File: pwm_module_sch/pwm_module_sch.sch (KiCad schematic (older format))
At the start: 49 parts, among them J1 SWIMM, J2 output -, J3 input, J4 output+, J5 uart, Q1 AO3400, Q2 6N60, SW1 ., SW2 ., U1 TM1637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

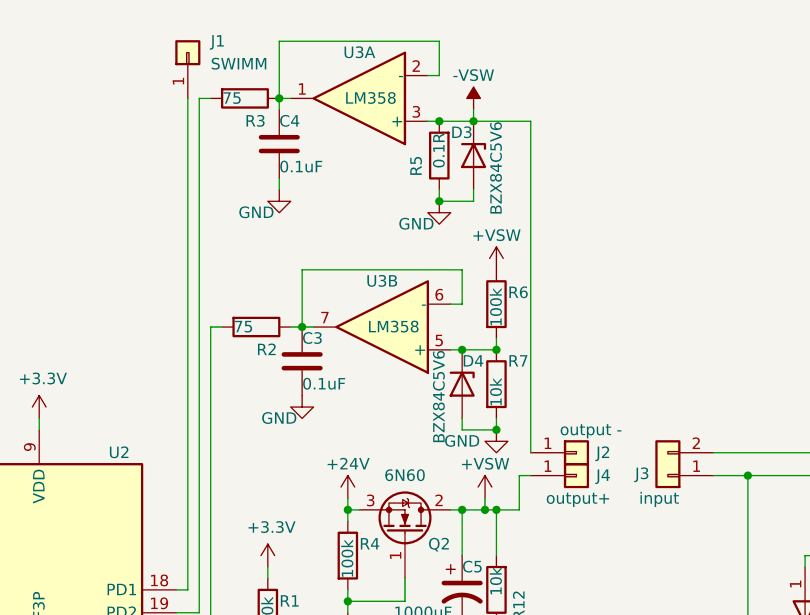
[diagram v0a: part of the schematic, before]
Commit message: 10A shunt
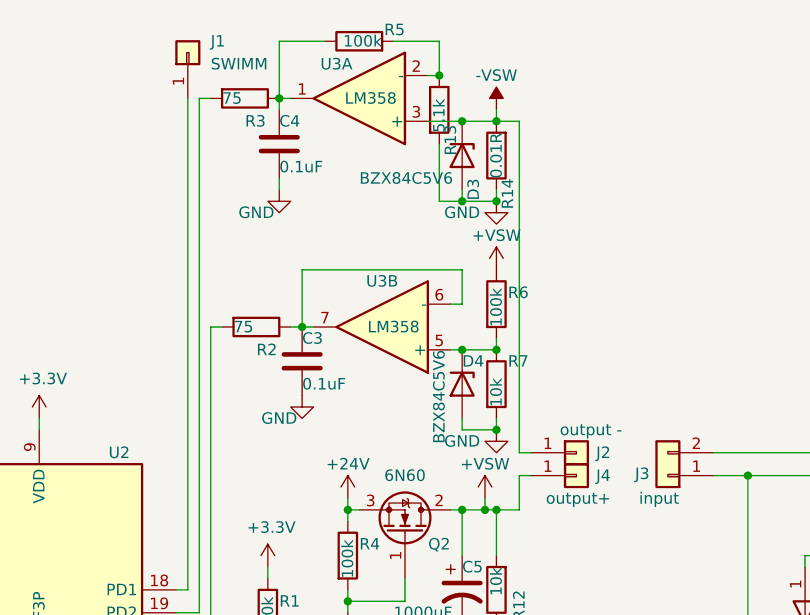
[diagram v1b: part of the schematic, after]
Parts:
- added R13: 5.1k, Resistor_SMD:R_0805_2012Metric, symbol Device:R
- added R14: 0.01R, Resistor_THT:R_Bare_Metal_Element_L12.4mm_W4.8mm_P11.40mm, symbol Device:R
- R5: value 0.1R -> 100k; footprint Resistor_SMD:R_1210_3225Metric -> Resistor_SMD:R_0402_1005Metric
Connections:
- net -VSW: now also R14.2; no longer R5.2
- net GND: now also R13.2, R14.1; no longer R5.1
- net at C4.1, R3.1, U3.1: now also R5.1; no longer U3.2 (-)
- new net: R13.1, R5.2, U3.2 (-)
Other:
- moved on the sheet: D3
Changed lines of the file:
@@
 U 1 1 62109DDC
 P 4750 800
-F 0 "U3" H 4750 600 50  0000 C CNN
+F 0 "U3" H 4850 650 50  0000 C CNN
 F 1 "LM358" H 4700 800 50  0000 C CNN
 F 2 "Package_SO:SO-8_3.9x4.9mm_P1.27mm" H 4750 800 50  0001 C CNN
@@
 	5100 700  5100 550
 Wire Wire Line
-	5100 550  4400 550
-Wire Wire Line
 	4400 550  4400 800
 Wire Wire Line
 	4400 800  4450 800
-$Comp
-L Device:R R5
-U 1 1 62070859
-P 5100 1050
-F 0 "R5" V 5200 1050 50  0000 L CNN
-F 1 "0.1R" V 5100 950 50  0000 L CNN
-F 2 "Resistor_SMD:R_1210_3225Metric" V 5030 1050 50  0001 C CNN
-F 3 "~" H 5100 1050 50  0001 C CNN
-	1    5100 1050
-	-1   0    0    1
-$EndComp
-Wire Wire Line
-	5100 900  5050 900
 $Comp
 L power:GND #PWR0107
 U 1 1 6208BD4F
-P 5100 1250
-F 0 "#PWR0107" H 5100 1000 50  0001 C CNN
-F 1 "GND" H 5000 1150 50  0000 C CNN
-F 2 "" H 5100 1250 50  0001 C CNN
-F 3 "" H 5100 1250 50  0001 C CNN
-	1    5100 1250
+P 5350 1250
+F 0 "#PWR0107" H 5350 1000 50  0001 C CNN
+F 1 "GND" H 5200 1200 50  0000 C CNN
+F 2 "" H 5350 1250 50  0001 C CNN
+F 3 "" H 5350 1250 50  0001 C CNN
+	1    5350 1250
 	1    0    0    -1
 $EndComp
@@
 L power:-VSW #PWR0132
 U 1 1 6210BE8B
-P 5250 850
-F 0 "#PWR0132" H 5250 950 50  0001 C CNN
-F 1 "-VSW" H 5250 1000 50  0000 C CNN
-F 2 "" H 5250 850 50  0001 C CNN
-F 3 "" H 5250 850 50  0001 C CNN
-	1    5250 850
+P 5350 850
+F 0 "#PWR0132" H 5350 950 50  0001 C CNN
+F 1 "-VSW" H 5350 1000 50  0000 C CNN
+F 2 "" H 5350 850 50  0001 C CNN
+F 3 "" H 5350 850 50  0001 C CNN
+	1    5350 850
 	1    0    0    -1
 $EndComp
@@
 L Diode:BZX84Cxx D3
 U 1 1 622739ED
-P 5250 1050
-F 0 "D3" V 5150 950 50  0000 L CNN
-F 1 "BZX84C5V6" H 5100 1150 50  0000 L CNN
-F 2 "Diode_SMD:D_SOT-23_ANK" H 5250 875 50  0001 C CNN
-F 3 "https://diotec.com/tl_files/diotec/files/pdf/datasheets/bzx84c2v4.pdf" H 5250 1050 50  0001 C CNN
-	1    5250 1050
+P 5200 1050
+F 0 "D3" H 5300 1100 50  0000 L CNN
+F 1 "BZX84C5V6" V 5300 600 50  0000 L CNN
+F 2 "Diode_SMD:D_SOT-23_ANK" H 5200 875 50  0001 C CNN
+F 3 "https://diotec.com/tl_files/diotec/files/pdf/datasheets/bzx84c2v4.pdf" H 5200 1050 50  0001 C CNN
+	1    5200 1050
 	0    1    1    0
 $EndComp
-Wire Wire Line
-	5100 900  5250 900
-Connection ~ 5100 900
-Wire Wire Line
-	5100 1200 5100 1250
-Wire Wire Line
-	5250 1200 5250 1250
-Wire Wire Line
-	5250 1250 5100 1250
-Connection ~ 5100 1250
-Connection ~ 5250 900
 $Comp
 L Device:C C4
@@
 	1    0    0    -1
 $EndComp
-Wire Wire Line
-	5250 900  5250 850
 Wire Wire Line
 	2400 4300 2400 4200
@@
 	4050 800  4050 3050
 Wire Wire Line
-	5500 900  5500 2350
-Wire Wire Line
-	5250 900  5500 900
-Wire Wire Line
 	4000 800  4000 2950
+$Comp
+L Device:R R14
+U 1 1 622FAFE9
+P 5350 1050
+F 0 "R14" V 5300 1150 50  0000 L CNN
+F 1 "0.01R" V 5350 950 50  0000 L CNN
+F 2 "Resistor_THT:R_Bare_Metal_Element_L12.4mm_W4.8mm_P11.40mm" V 5280 1050 50  0001 C CNN
+F 3 "~" H 5350 1050 50  0001 C CNN
+	1    5350 1050
+	-1   0    0    1
+$EndComp
+Connection ~ 5200 900
+Wire Wire Line
+	5200 1200 5200 1250
+Wire Wire Line
+	5450 2350 5500 2350
+Wire Wire Line
+	5200 900  5350 900
+Wire Wire Line
+	5450 900  5450 2350
+$Comp
+L Device:R R5
+U 1 1 62418FC9
+P 4750 550
+F 0 "R5" V 4800 350 50  0000 L CNN
+F 1 "100k" V 4750 450 50  0000 L CNN
+F 2 "Resistor_SMD:R_0402_1005Metric" V 4680 550 50  0001 C CNN
+F 3 "~" H 4750 550 50  0001 C CNN
+	1    4750 550
+	0    -1   -1   0
+$EndComp
+Connection ~ 5350 900
+Wire Wire Line
+	5350 900  5450 900
+Wire Wire Line
+	5200 1250 5350 1250
+Wire Wire Line
+	5050 900  5200 900
+Wire Wire Line
+	5350 1250 5350 1200
+Connection ~ 5350 1250
+$Comp
+L Device:R R13
+U 1 1 62467885
+P 5100 850
+F 0 "R13" V 5150 650 50  0000 L CNN
+F 1 "5.1k" V 5100 750 50  0000 L CNN
+F 2 "Resistor_SMD:R_0805_2012Metric" V 5030 850 50  0001 C CNN
+F 3 "~" H 5100 850 50  0001 C CNN
+	1    5100 850
+	1    0    0    -1
+$EndComp
+Connection ~ 5100 700
+Wire Wire Line
+	5100 1000 5100 1250
+Wire Wire Line
+	5100 1250 5200 1250
+Connection ~ 5200 1250
+Wire Wire Line
+	5350 900  5350 850
+Wire Wire Line
+	4400 550  4600 550
+Wire Wire Line
+	4900 550  5100 550
 $EndSCHEMATC

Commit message: board ok
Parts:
- Q2: value 6N60 -> IRFZ44N
- R12: footprint Resistor_SMD:R_1210_3225Metric -> Resistor_SMD:R_1206_3216Metric
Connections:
- net GND: now also R13.1; no longer R13.2
- net at R5.2, U3.2 (-): now also R13.2; no longer R13.1
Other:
- moved on the sheet: C7, C8, C9, D3, D8, R13, R14, R8, U4

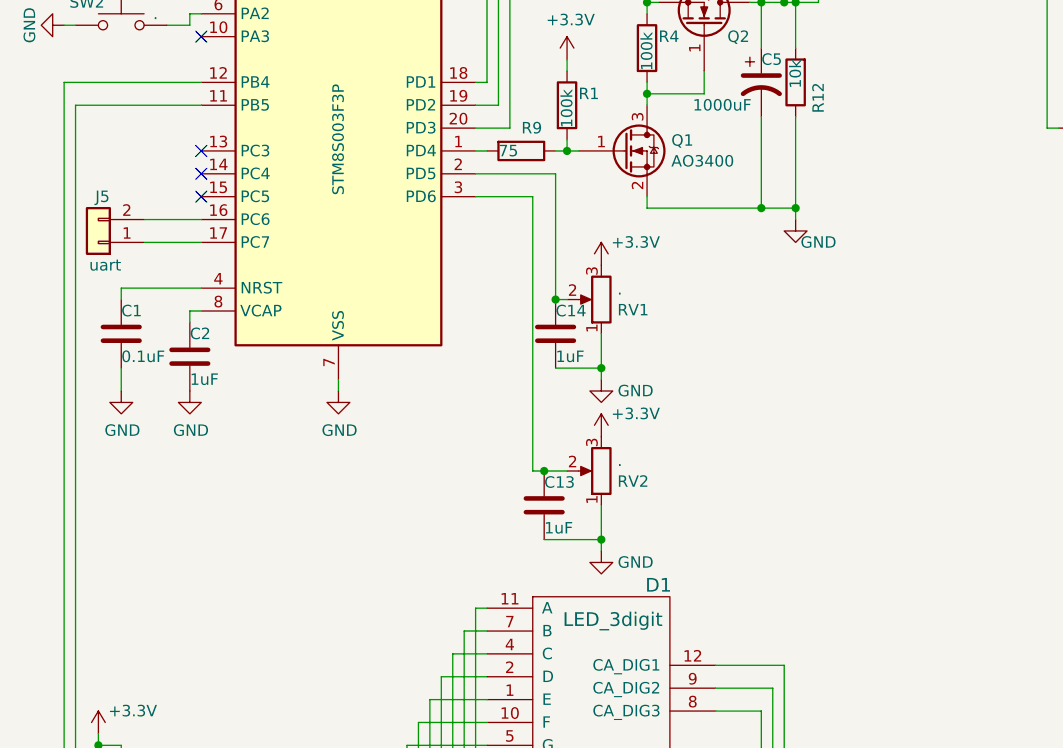
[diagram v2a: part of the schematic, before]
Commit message: working UART on board
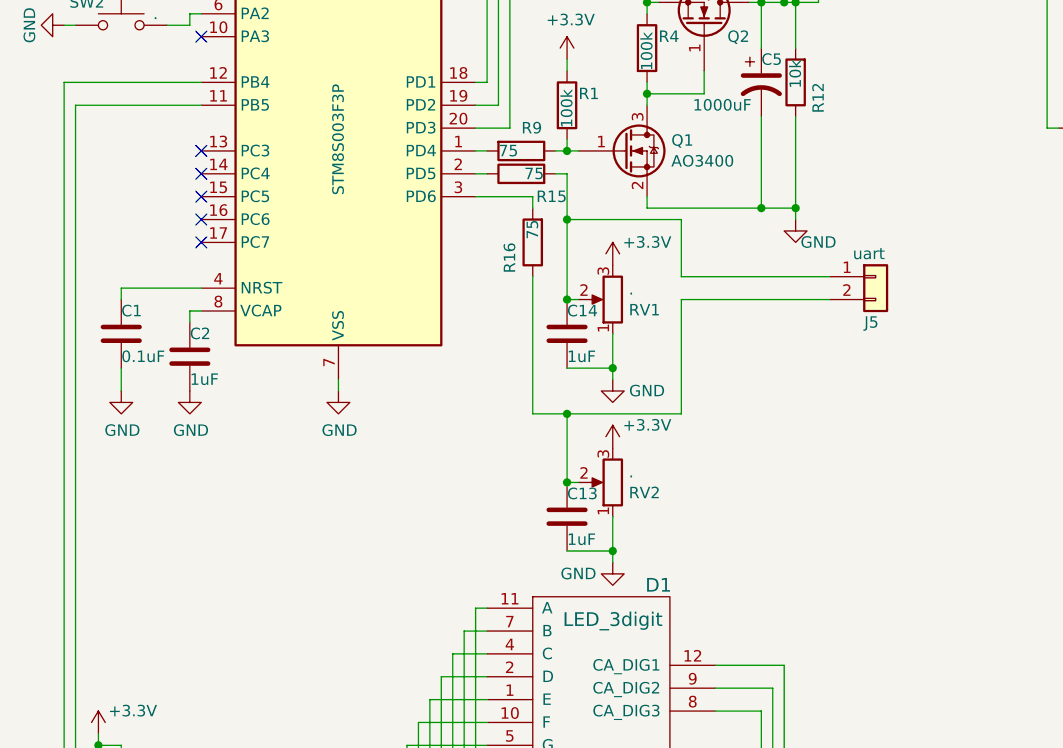
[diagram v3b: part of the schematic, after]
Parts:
- added R15, R16: 75, Resistor_SMD:R_0402_1005Metric, symbol Device:R
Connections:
- net at U2.16 (PC6): no longer J5.2 (Pin_2)
- net at U2.17 (PC7): no longer J5.1 (Pin_1)
- net at C14.1, RV1.2: now also J5.1 (Pin_1), R15.2; no longer U2.2 (PD5)
- net at C13.1, RV2.2: now also J5.2 (Pin_2), R16.1; no longer U2.3 (PD6)
- new net: R15.1, U2.2 (PD5)
- new net: R16.2, U2.3 (PD6)
- no-connect marks 6 -> 8
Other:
- moved on the sheet: C13, C14, J5, RV1, RV2
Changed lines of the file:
@@
 L power:GND #PWR0105
 U 1 1 620B76D5
-P 4500 4250
-F 0 "#PWR0105" H 4500 4000 50  0001 C CNN
-F 1 "GND" H 4650 4200 50  0000 C CNN
-F 2 "" H 4500 4250 50  0001 C CNN
-F 3 "" H 4500 4250 50  0001 C CNN
-	1    4500 4250
+P 4550 4250
+F 0 "#PWR0105" H 4550 4000 50  0001 C CNN
+F 1 "GND" H 4700 4200 50  0000 C CNN
+F 2 "" H 4550 4250 50  0001 C CNN
+F 3 "" H 4550 4250 50  0001 C CNN
+	1    4550 4250
 	1    0    0    -1
 $EndComp
@@
 L Device:R_Potentiometer RV1
 U 1 1 620D21AF
-P 4500 3900
-F 0 "RV1" H 4430 3946 50  0000 R CNN
-F 1 "." H 4430 3855 50  0000 R CNN
-F 2 "pwm_module:SP3-4" H 4500 3900 50  0001 C CNN
-F 3 "~" H 4500 3900 50  0001 C CNN
-	1    4500 3900
+P 4550 3900
+F 0 "RV1" H 4480 3946 50  0000 R CNN
+F 1 "." H 4480 3855 50  0000 R CNN
+F 2 "pwm_module:SP3-4" H 4550 3900 50  0001 C CNN
+F 3 "~" H 4550 3900 50  0001 C CNN
+	1    4550 3900
 	-1   0    0    1
 $EndComp
@@
 L Device:R_Potentiometer RV2
 U 1 1 620D31F7
-P 4500 4650
-F 0 "RV2" H 4430 4696 50  0000 R CNN
-F 1 "." H 4430 4605 50  0000 R CNN
-F 2 "pwm_module:SP3-4" H 4500 4650 50  0001 C CNN
-F 3 "~" H 4500 4650 50  0001 C CNN
-	1    4500 4650
+P 4550 4700
+F 0 "RV2" H 4480 4746 50  0000 R CNN
+F 1 "." H 4480 4655 50  0000 R CNN
+F 2 "pwm_module:SP3-4" H 4550 4700 50  0001 C CNN
+F 3 "~" H 4550 4700 50  0001 C CNN
+	1    4550 4700
 	-1   0    0    1
 $EndComp
@@
 L power:+3.3V #PWR0114
 U 1 1 622371EC
-P 4500 3750
-F 0 "#PWR0114" H 4500 3600 50  0001 C CNN
-F 1 "+3.3V" H 4650 3850 50  0000 C CNN
-F 2 "" H 4500 3750 50  0001 C CNN
-F 3 "" H 4500 3750 50  0001 C CNN
-	1    4500 3750
+P 4550 3750
+F 0 "#PWR0114" H 4550 3600 50  0001 C CNN
+F 1 "+3.3V" H 4700 3850 50  0000 C CNN
+F 2 "" H 4550 3750 50  0001 C CNN
+F 3 "" H 4550 3750 50  0001 C CNN
+	1    4550 3750
 	1    0    0    -1
 $EndComp
@@
 L power:+3.3V #PWR0115
 U 1 1 6223863E
-P 4500 4500
-F 0 "#PWR0115" H 4500 4350 50  0001 C CNN
-F 1 "+3.3V" H 4650 4600 50  0000 C CNN
-F 2 "" H 4500 4500 50  0001 C CNN
-F 3 "" H 4500 4500 50  0001 C CNN
-	1    4500 4500
+P 4550 4550
+F 0 "#PWR0115" H 4550 4400 50  0001 C CNN
+F 1 "+3.3V" H 4700 4650 50  0000 C CNN
+F 2 "" H 4550 4550 50  0001 C CNN
+F 3 "" H 4550 4550 50  0001 C CNN
+	1    4550 4550
 	1    0    0    -1
 $EndComp
@@
 L power:GND #PWR0117
 U 1 1 6223B781
-P 4500 5000
-F 0 "#PWR0117" H 4500 4750 50  0001 C CNN
-F 1 "GND" H 4650 4950 50  0000 C CNN
-F 2 "" H 4500 5000 50  0001 C CNN
-F 3 "" H 4500 5000 50  0001 C CNN
-	1    4500 5000
-	1    0    0    -1
-$EndComp
-Wire Wire Line
-	4350 3900 4300 3900
+P 4550 5050
+F 0 "#PWR0117" H 4550 4800 50  0001 C CNN
+F 1 "GND" H 4400 5000 50  0000 C CNN
+F 2 "" H 4550 5050 50  0001 C CNN
+F 3 "" H 4550 5050 50  0001 C CNN
+	1    4550 5050
+	1    0    0    -1
+$EndComp
+Wire Wire Line
+	4400 3900 4350 3900
 Wire Wire Line
 	3950 3450 4200 3450
-Wire Wire Line
-	4250 4650 4350 4650
 Wire Wire Line
 	4100 3150 3950 3150
@@
 	1    0    0    -1
 $EndComp
-$Comp
-L Device:C C13
-U 1 1 62262A8F
-P 4250 4800
-F 0 "C13" H 4250 4900 50  0000 L CNN
-F 1 "1uF" H 4250 4700 50  0000 L CNN
-F 2 "Capacitor_SMD:C_0805_2012Metric" H 4288 4650 50  0001 C CNN
-F 3 "~" H 4250 4800 50  0001 C CNN
-	1    4250 4800
-	1    0    0    -1
-$EndComp
-Wire Wire Line
-	4250 4950 4500 4950
-Wire Wire Line
-	4500 4950 4500 5000
-Wire Wire Line
-	4500 4950 4500 4800
-Connection ~ 4500 4950
+Wire Wire Line
+	4550 5000 4550 5050
+Wire Wire Line
+	4550 5000 4550 4850
+Connection ~ 4550 5000
 $Comp
 L Device:C C14
 U 1 1 622C31D5
-P 4300 4050
-F 0 "C14" H 4300 4150 50  0000 L CNN
-F 1 "1uF" H 4300 3950 50  0000 L CNN
-F 2 "Capacitor_SMD:C_0805_2012Metric" H 4338 3900 50  0001 C CNN
-F 3 "~" H 4300 4050 50  0001 C CNN
-	1    4300 4050
-	1    0    0    -1
-$EndComp
-Wire Wire Line
-	4300 4200 4500 4200
-Wire Wire Line
-	4500 4200 4500 4250
-Wire Wire Line
-	4500 4200 4500 4050
-Connection ~ 4500 4200
-Wire Wire Line
-	4250 4650 4200 4650
-Connection ~ 4250 4650
+P 4350 4050
+F 0 "C14" H 4350 4150 50  0000 L CNN
+F 1 "1uF" H 4350 3950 50  0000 L CNN
+F 2 "Capacitor_SMD:C_0805_2012Metric" H 4388 3900 50  0001 C CNN
+F 3 "~" H 4350 4050 50  0001 C CNN
+	1    4350 4050
+	1    0    0    -1
+$EndComp
+Wire Wire Line
+	4350 4200 4550 4200
+Wire Wire Line
+	4550 4200 4550 4250
+Wire Wire Line
+	4550 4200 4550 4050
+Connection ~ 4550 4200
 Wire Wire Line
 	2150 2950 2150 6350
@@
 	2200 3050 2200 6250
 Wire Wire Line
-	4200 3450 4200 4650
+	4200 3450 4200 3500
 Wire Wire Line
 	4000 3250 3950 3250
@@
 	4700 3500 5200 3500
 Wire Wire Line
-	4300 3900 4300 3350
-Wire Wire Line
-	4300 3350 3950 3350
-Connection ~ 4300 3900
+	4350 3900 4350 3550
+Connection ~ 4350 3900
 Wire Wire Line
 	7900 3450 7900 3400
@@
 L Connector_Generic:Conn_01x02 J5
 U 1 1 621F9B6F
-P 2300 3650
-F 0 "J5" H 2250 3450 50  0000 L CNN
-F 1 "uart" H 2200 3750 50  0000 L CNN
-F 2 "Connector_PinHeader_2.54mm:PinHeader_1x02_P2.54mm_Vertical" H 2300 3650 50  0001 C CNN
-F 3 "~" H 2300 3650 50  0001 C CNN
-	1    2300 3650
-	-1   0    0    1
+P 5700 3800
+F 0 "J5" H 5650 3600 50  0000 L CNN
+F 1 "uart" H 5600 3900 50  0000 L CNN
+F 2 "Connector_PinHeader_2.54mm:PinHeader_1x02_P2.54mm_Vertical" H 5700 3800 50  0001 C CNN
+F 3 "~" H 5700 3800 50  0001 C CNN
+	1    5700 3800
+	1    0    0    -1
 $EndComp
 $Comp
@@
 Wire Wire Line
 	5200 3500 5350 3500
-Wire Wire Line
-	2500 3550 2750 3550
-Wire Wire Line
-	2500 3650 2750 3650
 $Comp
 L Device:C C3
@@
 Wire Wire Line
 	7400 3100 7500 3100
+Wire Wire Line
+	5500 3800 4850 3800
+Wire Wire Line
+	4850 3800 4850 3550
+Wire Wire Line
+	4850 3550 4350 3550
+Wire Wire Line
+	5500 3900 4850 3900
+Wire Wire Line
+	4850 3900 4850 4400
+NoConn ~ 2750 3550
+NoConn ~ 2750 3650
+$Comp
+L Device:R R16
+U 1 1 623DEA71
+P 4200 3650
+F 0 "R16" V 4300 3650 50  0000 L CNN
+F 1 "75" V 4200 3550 50  0000 L CNN
+F 2 "Resistor_SMD:R_0402_1005Metric" V 4130 3650 50  0001 C CNN
+F 3 "~" H 4200 3650 50  0001 C CNN
+	1    4200 3650
+	-1   0    0    1
+$EndComp
+Wire Wire Line
+	4200 3800 4200 4400
+$Comp
+L Device:R R15
+U 1 1 623E236F
+P 4150 3350
+F 0 "R15" V 4050 3150 50  0000 L CNN
+F 1 "75" V 4150 3250 50  0000 L CNN
+F 2 "Resistor_SMD:R_0402_1005Metric" V 4080 3350 50  0001 C CNN
+F 3 "~" H 4150 3350 50  0001 C CNN
+	1    4150 3350
+	0    -1   -1   0
+$EndComp
+Wire Wire Line
+	4000 3350 3950 3350
+Wire Wire Line
+	4300 3350 4350 3350
+Wire Wire Line
+	4350 3350 4350 3550
+Connection ~ 4350 3550
+$Comp
+L Device:C C13
+U 1 1 62262A8F
+P 4350 4850
+F 0 "C13" H 4350 4950 50  0000 L CNN
+F 1 "1uF" H 4350 4750 50  0000 L CNN
+F 2 "Capacitor_SMD:C_0805_2012Metric" H 4388 4700 50  0001 C CNN
+F 3 "~" H 4350 4850 50  0001 C CNN
+	1    4350 4850
+	1    0    0    -1
+$EndComp
+Wire Wire Line
+	4350 4700 4400 4700
+Wire Wire Line
+	4350 5000 4550 5000
+Wire Wire Line
+	4200 4400 4350 4400
+Wire Wire Line
+	4350 4700 4350 4400
+Connection ~ 4350 4700
+Connection ~ 4350 4400
+Wire Wire Line
+	4350 4400 4850 4400
 $EndSCHEMATC

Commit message: transistor
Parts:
- C5, C6: symbol Device:C_Polarized_US -> pwm_module_sch-rescue:C_Polarized_US-Device
- D5, D6, D7: symbol Device:D_Schottky_Dual_CommonCathode_AKA -> pwm_module_sch-rescue:D_Schottky_Dual_CommonCathode_AKA-Device
- RV1, RV2: symbol Device:R_Potentiometer -> pwm_module_sch-rescue:R_Potentiometer-Device
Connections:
- net +24V: now also Q2.2 (D); no longer Q2.3 (S)
- net +VSW: now also Q2.3 (S); no longer Q2.2 (D)
- net at R15.1, U2.2 (PD5): now also J5.1 (Pin_1)
- net at R16.2, U2.3 (PD6): now also J5.2 (Pin_2)
- net at D5.2 (K), J3.1 (Pin_1): now also D7.1 (A); no longer D7.3 (A)
- net at D6.2 (K), J3.2 (Pin_2): now also D7.3 (A); no longer D7.1 (A)
- net at C14.1, R15.2, RV1.2: no longer J5.1 (Pin_1)
- net at C13.1, R16.1, RV2.2: no longer J5.2 (Pin_2)
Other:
- moved on the sheet: R15, R16
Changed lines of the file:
@@
 U 1 1 620A7265
 P 4950 2700
-F 0 "Q2" V 4900 2850 50  0000 C CNN
+F 0 "Q2" V 4900 2550 50  0000 C CNN
 F 1 "IRFZ44N" V 5200 2700 50  0000 C CNN
 F 2 "Package_TO_SOT_THT:TO-220-3_Vertical" H 5150 2625 50  0001 L CIN
 F 3 "" H 4950 2700 50  0001 L CNN
 	1    4950 2700
-	0    1    -1   0
+	0    -1   -1   0
 $EndComp
 $Comp
@@
 $EndComp
 $Comp
-L Device:R_Potentiometer RV1
+L pwm_module_sch-rescue:R_Potentiometer-Device RV1
 U 1 1 620D21AF
 P 4550 3900
@@
 $EndComp
 $Comp
-L Device:R_Potentiometer RV2
+L pwm_module_sch-rescue:R_Potentiometer-Device RV2
 U 1 1 620D31F7
 P 4550 4700
@@
 	8800 4650 8800 4600
 $Comp
-L Device:D_Schottky_Dual_CommonCathode_AKA D5
+L pwm_module_sch-rescue:D_Schottky_Dual_CommonCathode_AKA-Device D5
 U 1 1 6205359E
 P 6700 3150
@@
 $EndComp
 $Comp
-L Device:D_Schottky_Dual_CommonCathode_AKA D6
+L pwm_module_sch-rescue:D_Schottky_Dual_CommonCathode_AKA-Device D6
 U 1 1 6207CB2A
 P 6900 3150
@@
 $EndComp
 $Comp
-L Device:D_Schottky_Dual_CommonCathode_AKA D7
+L pwm_module_sch-rescue:D_Schottky_Dual_CommonCathode_AKA-Device D7
 U 1 1 62058078
 P 7150 2800
@@
 F 3 "~" H 7150 2800 50  0001 C CNN
 	1    7150 2800
-	0    -1   -1   0
+	0    -1   1    0
 $EndComp
 Wire Wire Line
@@
 Connection ~ 7500 3100
 $Comp
-L Device:C_Polarized_US C6
+L pwm_module_sch-rescue:C_Polarized_US-Device C6
 U 1 1 62239E1E
 P 7400 3300
@@
 $EndComp
 $Comp
-L Device:C_Polarized_US C5
+L pwm_module_sch-rescue:C_Polarized_US-Device C5
 U 1 1 62166329
 P 5200 2950
@@
 $EndComp
 Wire Wire Line
-	6800 2800 6900 2800
-Wire Wire Line
 	3250 7550 5300 7550
 Wire Wire Line
@@
 	2200 3050 2200 6250
 Wire Wire Line
-	4200 3450 4200 3500
-Wire Wire Line
 	4000 3250 3950 3250
 $Comp
@@
 	4350 2900 4350 2850
 Wire Wire Line
-	4700 3450 4700 3500
-Wire Wire Line
 	4950 2900 4950 3000
 Wire Wire Line
@@
 Wire Wire Line
 	4700 2600 4700 2550
-Wire Wire Line
-	4700 3500 5200 3500
-Wire Wire Line
-	4350 3900 4350 3550
 Connection ~ 4350 3900
 Wire Wire Line
@@
 Wire Wire Line
 	5200 3100 5200 3500
-Connection ~ 5200 3500
 Wire Wire Line
 	5350 3100 5350 3500
@@
 L Device:R R16
 U 1 1 623DEA71
-P 4200 3650
-F 0 "R16" V 4300 3650 50  0000 L CNN
-F 1 "75" V 4200 3550 50  0000 L CNN
-F 2 "Resistor_SMD:R_0402_1005Metric" V 4130 3650 50  0001 C CNN
-F 3 "~" H 4200 3650 50  0001 C CNN
-	1    4200 3650
+P 4350 4550
+F 0 "R16" V 4450 4550 50  0000 L CNN
+F 1 "75" V 4350 4450 50  0000 L CNN
+F 2 "Resistor_SMD:R_0402_1005Metric" V 4280 4550 50  0001 C CNN
+F 3 "~" H 4350 4550 50  0001 C CNN
+	1    4350 4550
 	-1   0    0    1
 $EndComp
-Wire Wire Line
-	4200 3800 4200 4400
 $Comp
 L Device:R R15
 U 1 1 623E236F
-P 4150 3350
-F 0 "R15" V 4050 3150 50  0000 L CNN
-F 1 "75" V 4150 3250 50  0000 L CNN
-F 2 "Resistor_SMD:R_0402_1005Metric" V 4080 3350 50  0001 C CNN
-F 3 "~" H 4150 3350 50  0001 C CNN
-	1    4150 3350
-	0    -1   -1   0
-$EndComp
-Wire Wire Line
-	4000 3350 3950 3350
-Wire Wire Line
-	4300 3350 4350 3350
+P 4350 3750
+F 0 "R15" V 4250 3550 50  0000 L CNN
+F 1 "75" V 4350 3650 50  0000 L CNN
+F 2 "Resistor_SMD:R_0402_1005Metric" V 4280 3750 50  0001 C CNN
+F 3 "~" H 4350 3750 50  0001 C CNN
+	1    4350 3750
+	1    0    0    -1
+$EndComp
 Wire Wire Line
 	4350 3350 4350 3550
@@
 Wire Wire Line
 	4200 4400 4350 4400
-Wire Wire Line
-	4350 4700 4350 4400
 Connection ~ 4350 4700
 Connection ~ 4350 4400
 Wire Wire Line
 	4350 4400 4850 4400
+Wire Wire Line
+	4200 3450 4200 4400
+Wire Wire Line
+	4350 3600 4350 3550
+Wire Wire Line
+	3950 3350 4350 3350
+Wire Wire Line
+	4700 3450 4700 3500
+Wire Wire Line
+	4700 3500 5200 3500
+Connection ~ 5200 3500
+Wire Wire Line
+	6800 2800 6900 2800
 $EndSCHEMATC

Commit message: inductor
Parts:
- added D9: ., Package_TO_SOT_THT:TO-220-3_Vertical, symbol pwm_module_sch-rescue:D_Schottky_Dual_CommonCathode_AKA-Device-pwm_module_sch-r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
- added L1: 100uH, Inductor_THT:L_Toroid_Vertical_L24.6mm_W15.5mm_P11.44mm_Pulse_KM-4, symbol Device:L
- C5, C6: symbol pwm_module_sch-rescue:C_Polarized_US-Device -> pwm_module_sch-rescue:C_Polarized_US-Device-pwm_module_sch-rescue
- D5, D6, D7: symbol pwm_module_sch-rescue:D_Schottky_Dual_CommonCathode_AKA-Device -> pwm_module_sch-rescue:D_Schottky_Dual_CommonCathode_AKA-Device-pwm_module_sch-rescue
- RV1, RV2: symbol pwm_module_sch-rescue:R_Potentiometer-Device -> pwm_module_sch-rescue:R_Potentiometer-Device-pwm_module_sch-rescue
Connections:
- net +VSW: now also L1.2; no longer Q2.3 (S)
- net GND: now also D9.1 (A), D9.3 (A)
- new net: D9.2 (K), L1.1, Q2.3 (S)
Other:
- moved on the sheet: C10, C11, C12, C5, C6, C7, C8, C9, D5, D6, D7, D8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
